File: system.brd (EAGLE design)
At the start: 52.4 x 77 mm, 122 parts, among them IC1 TPS7B8650BQDDARQ1, J1 OLED, J2 163-179PH-EX, J3 AD2, J4 MCU, SW1 1825910-6, SW2 1825910-6, SW3 1825910-6, U1 ATMEGA328PB-AU, Y1 ABL-16.000MHZ-B2

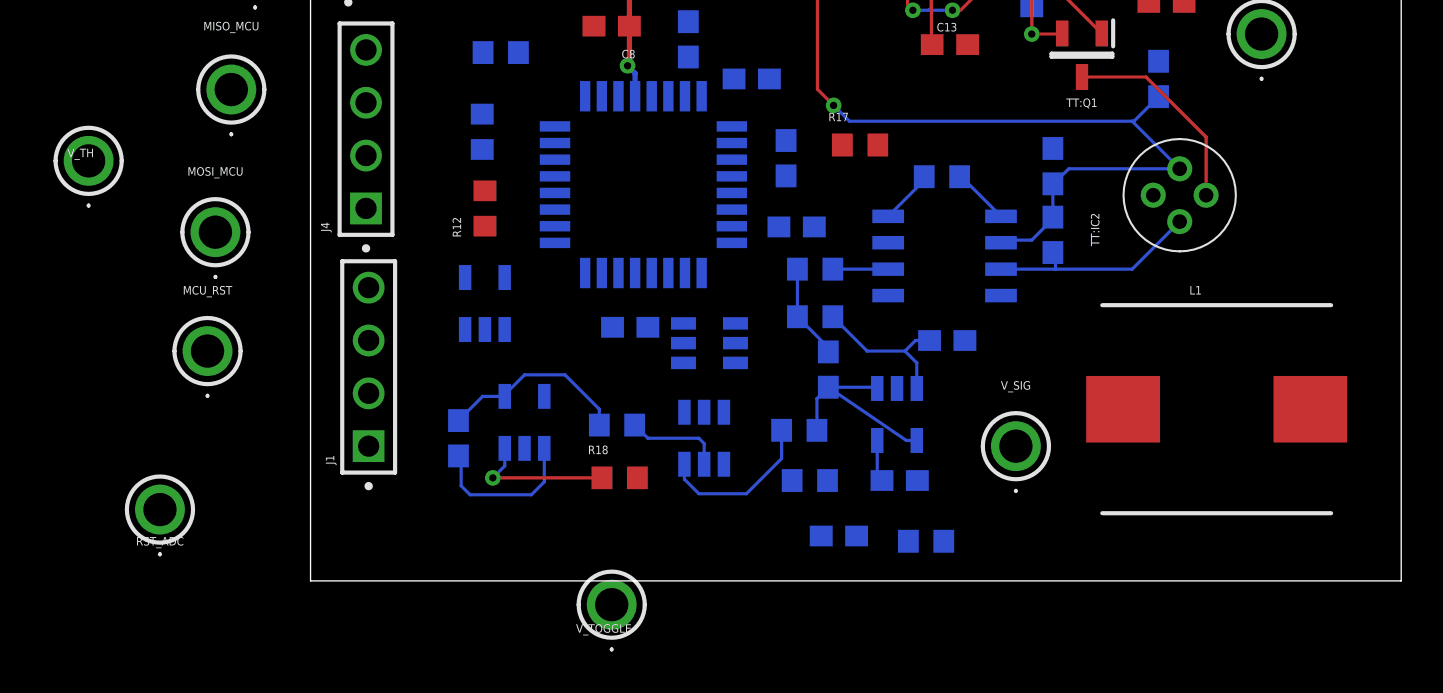
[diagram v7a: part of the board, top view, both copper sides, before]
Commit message: Wired ADC and AF parts PCB
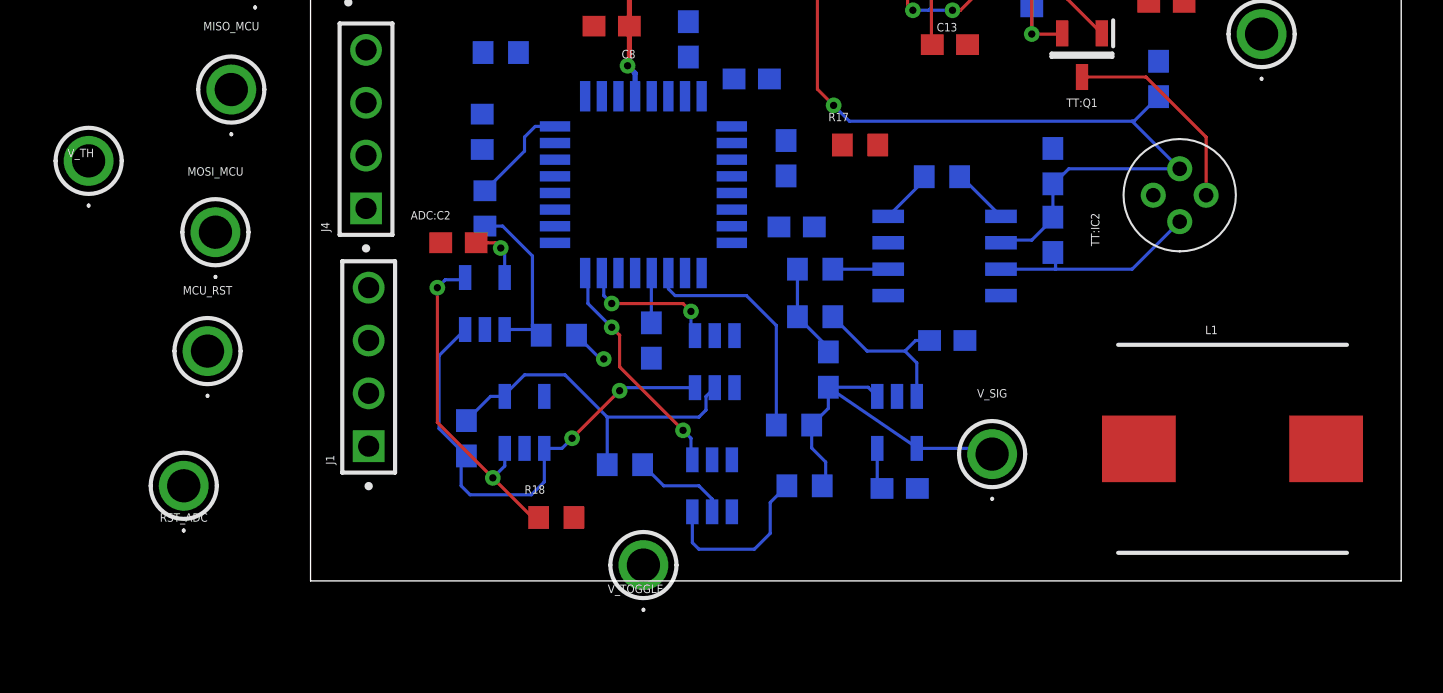
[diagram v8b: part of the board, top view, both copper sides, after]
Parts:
- moved ADC:C2 23.1 mm to (6.73, 7.49), flipped to the top
- moved ADC:R2 20.2 mm to (11.6, 3.05), turned to 0 degrees
- moved R18 3.59 mm to (11.4, -5.71)
- moved R19 2.77 mm to (22.9, -1.27)
- moved R16 2.68 mm to (23.4, -4.19)
- moved V_TOGGLE 2.44 mm to (15.6, -8.00)
- moved ADC:IC5 2.32 mm to (18.9, -4.19)
- moved L1 2.05 mm to (43.9, -2.41)
- moved ADC:R1 1.94 mm to (14.7, -3.17)
- moved RST_ADC 1.62 mm to (-6.48, -4.19)
- moved V_SIG 1.20 mm to (32.4, -2.67)
- moved C6 1.20 mm to (16.0, 2.79), turned to 270 degrees
- moved ADC:IC4 0.92 mm to (19.1, 1.78), turned to 270 degrees
- moved ADC:C1 0.38 mm to (7.11, -1.91)
- moved AF:IC2 0.38 mm to (27.8, -1.14)
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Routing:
- net ADC:N$2: track 7.53 -> 23.2 mm, vias 0 -> 2
- net V_SIG_ADC: track 0.00 -> 11.5 mm
- net V_TOGGLE: track 0.00 -> 11.1 mm, vias 0 -> 2
- net N$5: track 6.90 -> 16.4 mm, vias 1 -> 2
- net N$14: track 0.00 -> 8.73 mm
- net ADC:N$4: track 9.18 -> 17.0 mm
- net V_SIG: track 9.72 -> 16.9 mm
- net RST_ADC: track 0.00 -> 6.87 mm, vias 0 -> 2
- net N$6: track 0.00 -> 5.11 mm, vias 0 -> 2
- net ADC_EXT_INT: track 0.00 -> 5.05 mm
- net N$15: track 0.00 -> 2.40 mm
- net N$2: track 7.74 -> 8.29 mm
